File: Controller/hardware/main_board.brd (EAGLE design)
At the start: 75 x 59 mm, 45 parts, among them IC1 LINEAR_78DT, IC2 40XX_4050D, IC3 LP298XS, IC5 ATMEGA328, Q4 16MHZ, X1 MICROSD_SMD, X4 CON-PHOENIX-508_MST2V

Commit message: new 16mhz crystal with internal caps
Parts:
- removed C12, C13: 16pF, main_board:SPARKFUN_0805
- removed Q4: 16MHZ, main_board:CRYSTAL_HC49/S
- added U1: CSTNE16M0VH3L000R0, main_board:XTAL_CSTNE16M0VH3L000R0
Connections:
- removed net N$31: C12.2, IC5.7, Q4.2
- removed net N$32: C13.2, IC5.8, Q4.1
- new net N$22: IC5.7, U1.1
- new net N$23: IC5.8, U1.3
- net GND: now also U1.2; no longer C12.1, C13.1
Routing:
- net N$31: track 18.4 -> 0.00 mm
- net N$32: track 13.7 -> 0.00 mm
- net N$22: track 0.00 -> 4.52 mm
- net N$23: track 0.00 -> 2.19 mm
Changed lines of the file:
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@@
 <attribute name="VENDOR_PN" value="732-4984-1-ND" x="8.01" y="12.13" size="1.778" layer="27" display="off"/>
-</element>
-<element name="C12" library="main_board" package="SPARKFUN_0805" value="16pF" x="26.62" y="19.38" smashed="yes" rot="R180">
-<attribute name="MFR" value="YAGEO" x="26.62" y="19.38" size="1.778" layer="27" rot="R180" display="off"/>
-<attribute name="MFR_PN" value="CC0805JRNPO9BN160" x="26.62" y="19.38" size="1.778" layer="27" rot="R180" display="off"/>
-<attribute name="NAME" x="25.082" y="19.7545" size="1.016" layer="25" rot="R180"/>
-<attribute name="VALUE" value="16pF" x="27.936" y="21.377" size="1.016" layer="27" rot="R180"/>
-<attribute name="VENDOR" value="digikey" x="26.62" y="19.38" size="1.778" layer="27" rot="R180" display="off"/>
-<attribute name="VENDOR_PN" value="311-4228-1-ND" x="26.62" y="19.38" size="1.778" layer="27" rot="R180" display="off"/>
-</element>
-<element name="C13" library="main_board" package="SPARKFUN_0805" value="16pF" x="31.37" y="19.42" smashed="yes">
-<attribute name="MFR" value="YAGEO" x="31.37" y="19.42" size="1.778" layer="27" display="off"/>
-<attribute name="MFR_PN" value="CC0805JRNPO9BN160" x="31.37" y="19.42" size="1.778" layer="27" display="off"/>
-<attribute name="NAME" x="32.908" y="19.0455" size="1.016" layer="25"/>
-<attribute name="VALUE" value="16pF" x="29.954" y="20.723" size="1.016" layer="27"/>
-<attribute name="VENDOR" value="digikey" x="31.37" y="19.42" size="1.778" layer="27" display="off"/>
-<attribute name="VENDOR_PN" value="311-4228-1-ND" x="31.37" y="19.42" size="1.778" layer="27" display="off"/>
 </element>
 <element name="C14" library="main_board" package="SPARKFUN_0805" value="0.1uF" x="45.44" y="30.48" smashed="yes" rot="R180">
@@
 <attribute name="MFR" value="Samsung Electro-Mechanics" x="30.2" y="29.58" size="1.778" layer="27" rot="R180" display="off"/>
 <attribute name="MFR_PN" value="CL21B104KBCNFNC" x="30.2" y="29.58" size="1.778" layer="27" rot="R180" display="off"/>
-<attribute name="NAME" x="30.962" y="28.5545" size="1.016" layer="25" rot="R180"/>
+<attribute name="NAME" x="30.762" y="28.6545" size="1.016" layer="25" rot="R180"/>
 <attribute name="VALUE" value="0.1uF" x="31.216" y="30.977" size="1.016" layer="27" rot="R180"/>
 <attribute name="VENDOR" value="digikey" x="30.2" y="29.58" size="1.778" layer="27" rot="R180" display="off"/>
@@
 <attribute name="VALUE" x="41.77" y="13.925" size="1.27" layer="27" rot="R180"/>
 </element>
-<element name="Q4" library="main_board" package="CRYSTAL_HC49/S" value="16MHZ" x="29.01" y="15.53" smashed="yes" rot="R180">
-<attribute name="MFR" value="IQD Frequency Products" x="29.01" y="15.53" size="1.778" layer="27" rot="R180" display="off"/>
-<attribute name="MFR_PN" value="LFXTAL003240BULK" x="29.01" y="15.53" size="1.778" layer="27" rot="R180" display="off"/>
-<attribute name="NAME" x="29.363" y="18.21" size="1.016" layer="25" ratio="10" rot="R90"/>
-<attribute name="VALUE" x="34.09" y="19.467" size="1.27" layer="27" ratio="10" rot="R180"/>
-<attribute name="VENDOR" value="digikey" x="29.01" y="15.53" size="1.778" layer="27" rot="R180" display="off"/>
-<attribute name="VENDOR_PN" value="1923-1433-ND" x="29.01" y="15.53" size="1.778" layer="27" rot="R180" display="off"/>
-</element>
 <element name="R1" library="main_board" package="ADAFRUIT_R0805" value="1.0k" x="4.52" y="12.21" smashed="yes" rot="R270">
 <attribute name="MFR" value="Stackpole Electronics Inc" x="4.52" y="12.21" size="1.778" layer="27" rot="R270" display="off"/>
@@
 <attribute name="VENDOR" value="digikey" x="21.9" y="10.8" size="1.778" layer="27" display="off"/>
 <attribute name="VENDOR_PN" value="1276-2402-1-ND" x="21.9" y="10.8" size="1.778" layer="27" display="off"/>
+</element>
+<element name="U1" library="main_board" package="XTAL_CSTNE16M0VH3L000R0" value="CSTNE16M0VH3L000R0" x="32" y="26" smashed="yes">
+<attribute name="DESCRIPTION" value=" 16MHz Ceramic Resonator Built in Capacitor 15pF ±0.11% 40 Ohms -40°C ~ 85°C Surface Mount " x="32" y="26" size="1.778" layer="27" display="off"/>
+<attribute name="MFR" value="Murata Electronics North America" x="32" y="26" size="1.778" layer="27" display="off"/>
+<attribute name="MFR_PN" value="CSTNE16M0VH3L000R0" x="32" y="26" size="1.778" layer="27" display="off"/>
+<attribute name="NAME" x="31.4" y="23.7" size="0.8128" layer="25"/>
+<attribute name="PACKAGE" value="SMD-3 Murata Electronics North America" x="32" y="26" size="1.778" layer="27" display="off"/>
+<attribute name="VALUE" x="29.8" y="23.4" size="0.8128" layer="27"/>
+<attribute name="VENDOR" value="Digikey" x="32" y="26" size="1.778" layer="27" display="off"/>
+<attribute name="VENDOR_PN" value="490-17952-1-ND" x="32" y="26" size="1.778" layer="27" display="off"/>
 </element>
 </elements>
@@
 </signal>
 <signal name="GND">
-<contactref element="C12" pad="1"/>
-<contactref element="C13" pad="1"/>
 <contactref element="C14" pad="1"/>
 <contactref element="C8" pad="1"/>
@@
 <contactref element="C4" pad="-"/>
 <contactref element="JP1" pad="3"/>
+<contactref element="U1" pad="2"/>
 </signal>
 <signal name="RX">
@@
 <wire x1="33.8684" y1="29.79" x2="34.28405" y2="30.20565" width="0.3048" layer="1"/>
 </signal>
-<signal name="N$31">
-<contactref element="C12" pad="2"/>
-<contactref element="Q4" pad="2"/>
-<contactref element="IC5" pad="7"/>
-<wire x1="25.7449" y1="16.8234" x2="25.7449" y2="19.3724" width="0.3048" layer="1"/>
-<wire x1="26.5096" y1="16.0587" x2="25.7449" y2="16.8234" width="0.3048" layer="1"/>
-<wire x1="26.5096" y1="15.5489" x2="26.5096" y2="16.0587" width="0.3048" layer="1"/>
-<wire x1="25.7449" y1="19.3724" x2="25.72" y2="19.38" width="0.3048" layer="1"/>
-<wire x1="26.5096" y1="15.5489" x2="26.597" y2="15.53" width="0.3048" layer="1"/>
-<wire x1="32.3" y1="28.93115" x2="33.137" y2="28.93115" width="0.3048" layer="1"/>
-<wire x1="33.137" y1="28.93115" x2="33.2074" y2="28.99" width="0.3048" layer="1"/>
-<wire x1="30.36885" y1="27" x2="32.3" y2="28.93115" width="0.3048" layer="1"/>
-<wire x1="25.72" y1="19.38" x2="27.34" y2="21" width="0.3048" layer="1"/>
-<wire x1="30.36885" y1="22.36885" x2="30.36885" y2="27" width="0.3048" layer="1"/>
-<wire x1="27.34" y1="21" x2="29" y2="21" width="0.3048" layer="1"/>
-<wire x1="29" y1="21" x2="30.36885" y2="22.36885" width="0.3048" layer="1"/>
-</signal>
-<signal name="N$32">
-<contactref element="C13" pad="2"/>
-<contactref element="Q4" pad="1"/>
-<contactref element="IC5" pad="8"/>
-<wire x1="32.24485" y1="16.69595" x2="32.24485" y2="19.3724" width="0.3048" layer="1"/>
-<wire x1="31.48015" y1="15.93125" x2="32.24485" y2="16.69595" width="0.3048" layer="1"/>
-<wire x1="31.48015" y1="15.5489" x2="31.48015" y2="15.93125" width="0.3048" layer="1"/>
-<wire x1="32.24485" y1="19.3724" x2="32.27" y2="19.42" width="0.3048" layer="1"/>
-<wire x1="31.48015" y1="15.5489" x2="31.423" y2="15.53" width="0.3048" layer="1"/>
-<wire x1="33.2074" y1="28.19" x2="32.67035" y2="28.19" width="0.3048" layer="1"/>
-<wire x1="32.67035" y1="28.19" x2="32.24485" y2="27.7645" width="0.3048" layer="1"/>
-<wire x1="32.24485" y1="19.49985" x2="32.24485" y2="27.7645" width="0.3048" layer="1"/>
-<wire x1="32.24485" y1="19.49985" x2="32.27" y2="19.42" width="0.3048" layer="1"/>
-</signal>
 <signal name="A3">
 <contactref element="IC5" pad="26"/>
@@
 <wire x1="66.7838" y1="48.431" x2="66.81" y2="48.35" width="1.016" layer="1"/>
 </signal>
+<signal name="N$22">
+<contactref element="U1" pad="1"/>
+<contactref element="IC5" pad="7"/>
+<wire x1="33.2074" y1="28.99" x2="32.29" y2="28.99" width="0.3048" layer="1"/>
+<wire x1="30.8" y1="27.5" x2="30.8" y2="26" width="0.3048" layer="1"/>
+<wire x1="32.29" y1="28.99" x2="30.8" y2="27.5" width="0.3048" layer="1"/>
+</signal>
+<signal name="N$23">
+<contactref element="IC5" pad="8"/>
+<contactref element="U1" pad="3"/>
+<wire x1="33.2" y1="26" x2="33.2" y2="28.1826" width="0.3048" layer="1"/>
+<wire x1="33.2" y1="28.1826" x2="33.2074" y2="28.19" width="0.3048" layer="1"/>
+</signal>
 </signals>

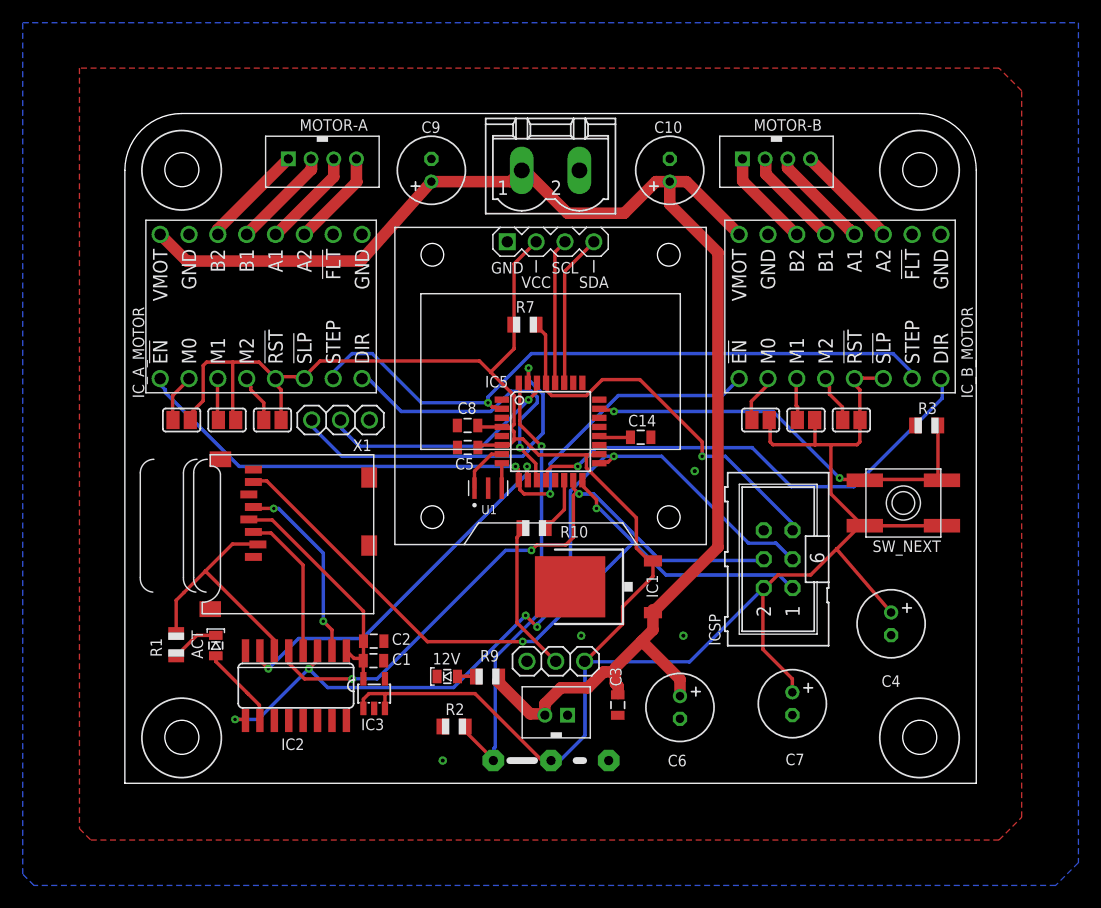
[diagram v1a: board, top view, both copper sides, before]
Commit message: working bypass capacitors
added bypass caps to the atmega328 and the 3v3 ldo per the datasheet. on the board relocated the 5v ldo bypass caps to be near the device itself.
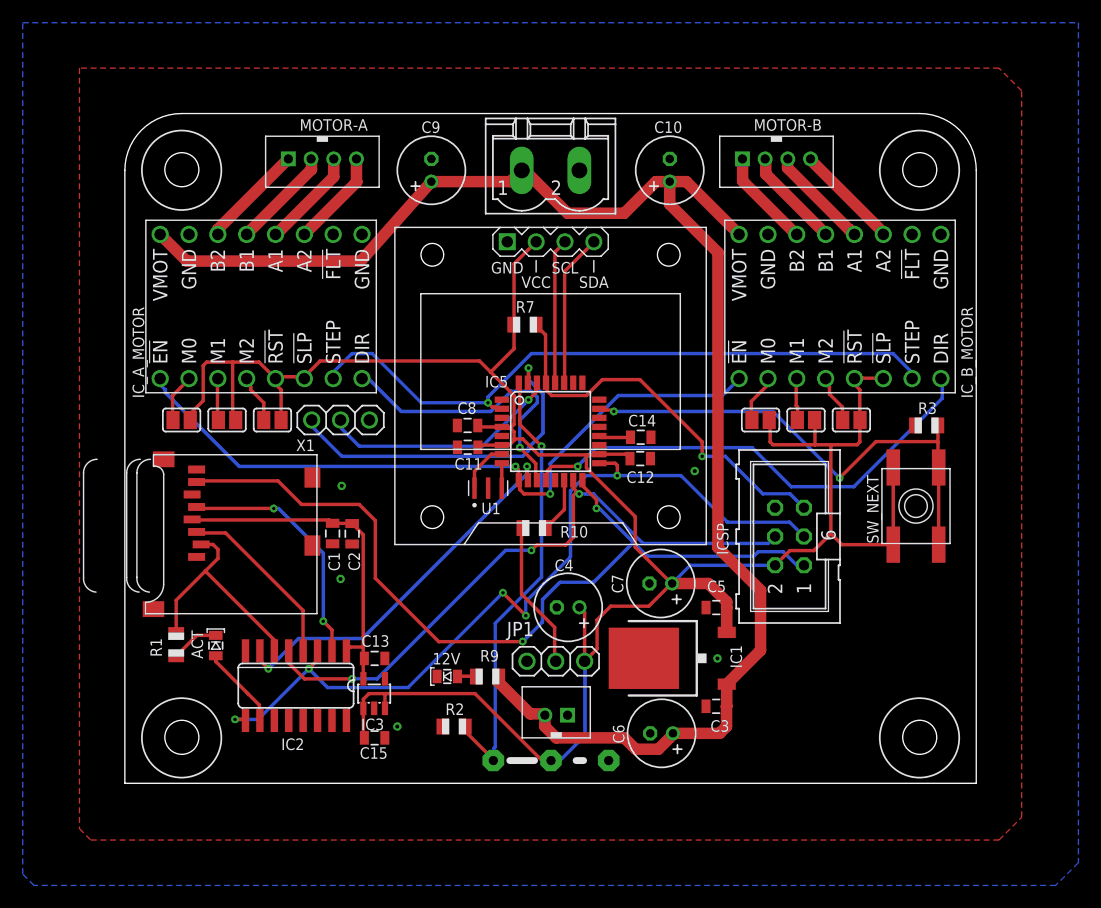
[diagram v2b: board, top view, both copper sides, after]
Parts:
- added C11, C12: 0.1uF, main_board:SPARKFUN_0805
- added C13: 2.2uF, main_board:SPARKFUN_0805
- added C15: 1.0uF, main_board:SPARKFUN_0805
- moved C4 28.5 mm to (39.0, 15.5), turned to 180 degrees
- moved C5 26.0 mm to (52.1, 15.5)
- moved C7 15.7 mm to (47.2, 17.6), turned to 180 degrees
- moved C1 11.8 mm to (18.3, 22.0), turned to 270 degrees
- moved C2 9.65 mm to (20.0, 22.0), turned to 270 degrees
- moved IC1 9.05 mm to (48.2, 11.0)
- moved C3 8.67 mm to (52.1, 6.78), turned to 180 degrees
- moved X1 5.00 mm to (17.0, 28.9)
- moved C6 2.80 mm to (47.3, 4.40), turned to 180 degrees
- moved ICSP 2.24 mm to (58.5, 21.7)
- moved SW_NEXT 1.14 mm to (69.7, 24.4), turned to 90 degrees
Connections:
- net +3V3: now also C13.2
- net GND: now also C11.1, C12.1, C13.1, C15.2
- net VCC: now also C11.2, C12.2, C15.1
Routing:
- net D12: track 66.2 -> 75.9 mm
- net A0: track 37.7 -> 46.3 mm
- net +3V3: track 21.8 -> 30.1 mm
- net +12V: track 131.6 -> 137.3 mm
- net N$2: track 16.8 -> 21.8 mm
- net VCC: track 215.9 -> 211.6 mm
- net N$5: track 13.2 -> 15.8 mm
- net N$3: track 21.7 -> 20.1 mm
- net D13: track 74.5 -> 73.9 mm
- net D11: track 56.4 -> 57.0 mm
